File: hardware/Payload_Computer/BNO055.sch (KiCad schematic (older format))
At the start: 8 parts

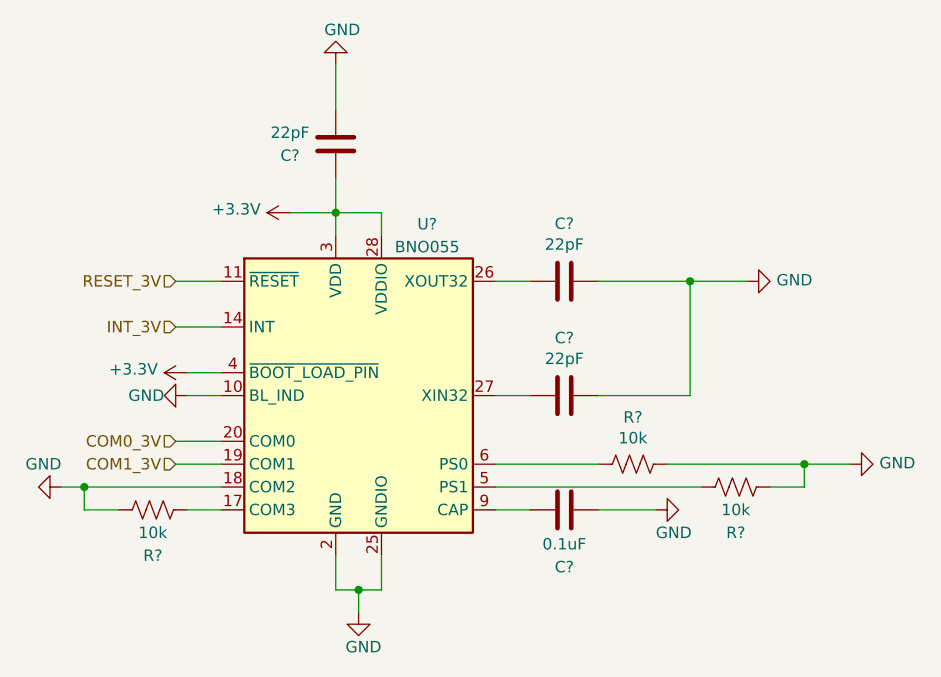
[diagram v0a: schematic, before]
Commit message: Finished BNO055
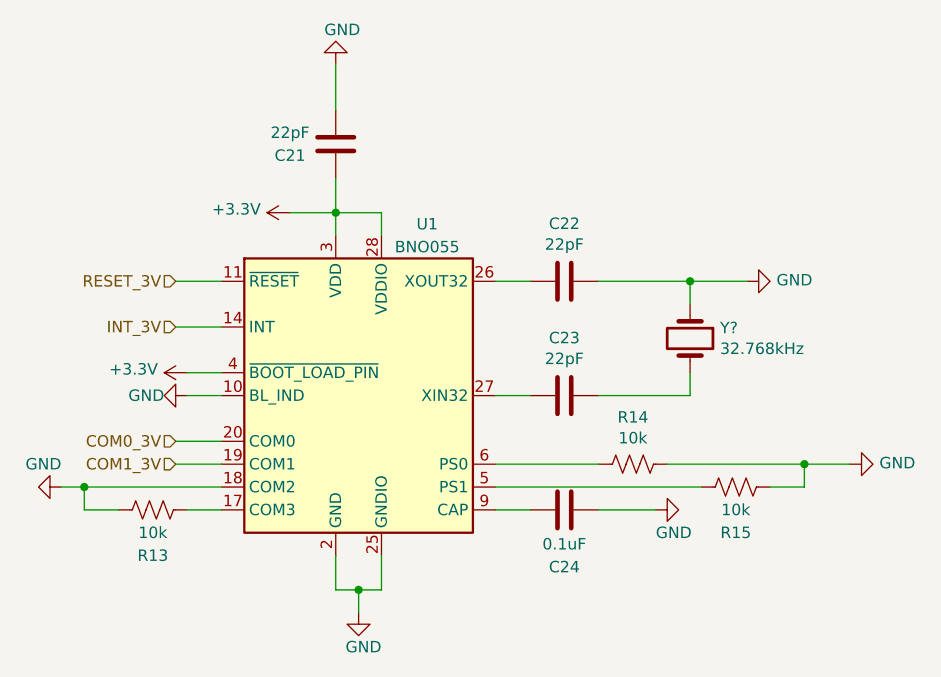
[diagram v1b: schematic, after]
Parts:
- added Y?: 32.768kHz, symbol Device:Crystal
- gave numbers to parts that had none: 8
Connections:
- net GND: now also Y?.1; no longer C23.1
- new net: C23.1, Y?.2
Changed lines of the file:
@@
 $Descr A4 11693 8268
 encoding utf-8
-Sheet 15 17
+Sheet 15 16
 Title ""
 Date ""
@@
 $EndDescr
 $Comp
-L Sensor_Motion:BNO055 U?
+L Sensor_Motion:BNO055 U1
 U 1 1 5F9DBC78
 P 5500 3750
-F 0 "U?" H 5800 4500 50  0000 C CNN
+F 0 "U1" H 5800 4500 50  0000 C CNN
 F 1 "BNO055" H 5800 4400 50  0000 C CNN
 F 2 "Package_LGA:LGA-28_5.2x3.8mm_P0.5mm" H 5750 3100 50  0001 L CNN
@@
 Connection ~ 6950 3250
 $Comp
-L power:GND #PWR?
+L power:GND #PWR0143
 U 1 1 5F9DBC80
 P 7200 3250
-F 0 "#PWR?" H 7200 3000 50  0001 C CNN
+F 0 "#PWR0143" H 7200 3000 50  0001 C CNN
 F 1 "GND" V 7205 3122 50  0000 R CNN
 F 2 "" H 7200 3250 50  0001 C CNN
@@
 Wire Wire Line
 	6100 3750 6250 3750
-Wire Wire Line
-	6950 3250 6950 3750
-$Comp
-L Device:C C?
+$Comp
+L Device:C C22
 U 1 1 5F9DBC88
 P 6400 3250
-F 0 "C?" V 6148 3250 50  0000 C CNN
+F 0 "C22" V 6148 3250 50  0000 C CNN
 F 1 "22pF" V 6239 3250 50  0000 C CNN
 F 2 "" H 6438 3100 50  0001 C CNN
@@
 $EndComp
 $Comp
-L Device:C C?
+L Device:C C24
 U 1 1 5F9DBC8E
 P 6400 4250
-F 0 "C?" V 6650 4250 50  0000 C CNN
+F 0 "C24" V 6650 4250 50  0000 C CNN
 F 1 "0.1uF" V 6550 4250 50  0000 C CNN
 F 2 "" H 6438 4100 50  0001 C CNN
@@
 	6550 4250 6800 4250
 $Comp
-L power:GND #PWR?
-U 1 1 5F9DBC99
-P 6800 4250
-F 0 "#PWR?" H 6800 4000 50  0001 C CNN
-F 1 "GND" V 6700 4250 50  0000 R CNN
-F 2 "" H 6800 4250 50  0001 C CNN
-F 3 "" H 6800 4250 50  0001 C CNN
-	1    6800 4250
-	0    -1   -1   0
-$EndComp
-$Comp
-L Device:R_US R?
+L Device:R_US R14
 U 1 1 5F9DBC9F
 P 6700 4050
-F 0 "R?" V 6495 4050 50  0000 C CNN
+F 0 "R14" V 6495 4050 50  0000 C CNN
 F 1 "10k" V 6586 4050 50  0000 C CNN
 F 2 "" V 6740 4040 50  0001 C CNN
@@
 $EndComp
 $Comp
-L Device:R_US R?
+L Device:R_US R15
 U 1 1 5F9DBCA5
 P 7150 4150
-F 0 "R?" V 7350 4150 50  0000 C CNN
+F 0 "R15" V 7350 4150 50  0000 C CNN
 F 1 "10k" V 7250 4150 50  0000 C CNN
 F 2 "" V 7190 4140 50  0001 C CNN
@@
 Connection ~ 7450 4050
 $Comp
-L power:GND #PWR?
+L power:GND #PWR0145
 U 1 1 5F9DBCB2
 P 7650 4050
-F 0 "#PWR?" H 7650 3800 50  0001 C CNN
+F 0 "#PWR0145" H 7650 3800 50  0001 C CNN
 F 1 "GND" V 7655 3922 50  0000 R CNN
 F 2 "" H 7650 4050 50  0001 C CNN
@@
 $EndComp
 $Comp
-L Device:C C?
+L Device:C C23
 U 1 1 5F9DBCB8
 P 6400 3750
-F 0 "C?" V 6148 3750 50  0000 C CNN
+F 0 "C23" V 6148 3750 50  0000 C CNN
 F 1 "22pF" V 6239 3750 50  0000 C CNN
 F 2 "" H 6438 3600 50  0001 C CNN
@@
 	4900 4150 4300 4150
 $Comp
-L power:GND #PWR?
+L power:GND #PWR0146
 U 1 1 5F9DBCBF
 P 4200 4150
-F 0 "#PWR?" H 4200 3900 50  0001 C CNN
+F 0 "#PWR0146" H 4200 3900 50  0001 C CNN
 F 1 "GND" V 4100 4150 50  0000 R CNN
 F 2 "" H 4200 4150 50  0001 C CNN
@@
 	4300 4150 4200 4150
 $Comp
-L Device:R_US R?
+L Device:R_US R13
 U 1 1 5F9DBCC9
 P 4600 4250
-F 0 "R?" V 4800 4250 50  0000 C CNN
+F 0 "R13" V 4800 4250 50  0000 C CNN
 F 1 "10k" V 4700 4250 50  0000 C CNN
 F 2 "" V 4640 4240 50  0001 C CNN
@@
 	4450 4250 4300 4250
 $Comp
-L Device:C C?
+L Device:C C21
 U 1 1 5F9DBCD0
 P 5400 2650
-F 0 "C?" H 5600 2700 50  0000 C CNN
+F 0 "C21" H 5600 2700 50  0000 C CNN
 F 1 "22pF" H 5600 2600 50  0000 C CNN
 F 2 "" H 5438 2500 50  0001 C CNN
@@
 $EndComp
 $Comp
-L power:GND #PWR?
+L power:GND #PWR0147
 U 1 1 5F9DBCD6
 P 5400 2300
-F 0 "#PWR?" H 5400 2050 50  0001 C CNN
+F 0 "#PWR0147" H 5400 2050 50  0001 C CNN
 F 1 "GND" H 5450 2150 50  0000 R CNN
 F 2 "" H 5400 2300 50  0001 C CNN
@@
 	5400 2950 5200 2950
 $Comp
-L power:+3.3V #PWR?
+L power:+3.3V #PWR0148
 U 1 1 5F9DBCE3
 P 5200 2950
-F 0 "#PWR?" H 5200 2800 50  0001 C CNN
+F 0 "#PWR0148" H 5200 2800 50  0001 C CNN
 F 1 "+3.3V" V 5215 3078 50  0000 L CNN
 F 2 "" H 5200 2950 50  0001 C CNN
@@
 	5500 4600 5600 4600
 $Comp
-L power:GND #PWR?
+L power:GND #PWR0149
 U 1 1 5F9DBCEF
 P 5500 4700
-F 0 "#PWR?" H 5500 4450 50  0001 C CNN
+F 0 "#PWR0149" H 5500 4450 50  0001 C CNN
 F 1 "GND" H 5600 4550 50  0000 R CNN
 F 2 "" H 5500 4700 50  0001 C CNN
@@
 	4900 3650 4750 3650
 $Comp
-L power:GND #PWR?
+L power:GND #PWR0150
 U 1 1 5F9DBCF7
 P 4750 3750
-F 0 "#PWR?" H 4750 3500 50  0001 C CNN
+F 0 "#PWR0150" H 4750 3500 50  0001 C CNN
 F 1 "GND" V 4750 3650 50  0000 R CNN
 F 2 "" H 4750 3750 50  0001 C CNN
@@
 $EndComp
 $Comp
-L power:+3.3V #PWR?
+L power:+3.3V #PWR0151
 U 1 1 5F9DBCFD
 P 4750 3650
-F 0 "#PWR?" H 4750 3500 50  0001 C CNN
+F 0 "#PWR0151" H 4750 3500 50  0001 C CNN
 F 1 "+3.3V" V 4765 3778 50  0000 L CNN
 F 2 "" H 4750 3650 50  0001 C CNN
@@
 Text HLabel 4700 4050 0    50   Input ~ 0
 COM1_3V
+Wire Wire Line
+	6950 3250 6950 3350
+$Comp
+L power:GND #PWR0144
+U 1 1 5F9DBC99
+P 6800 4250
+F 0 "#PWR0144" H 6800 4000 50  0001 C CNN
+F 1 "GND" V 6700 4250 50  0000 R CNN
+F 2 "" H 6800 4250 50  0001 C CNN
+F 3 "" H 6800 4250 50  0001 C CNN
+	1    6800 4250
+	0    -1   -1   0
+$EndComp
+$Comp
+L Device:Crystal Y?
+U 1 1 5FA07119
+P 6950 3500
+F 0 "Y?" V 6904 3631 50  0000 L CNN
+F 1 "32.768kHz" V 6995 3631 50  0000 L CNN
+F 2 "" H 6950 3500 50  0001 C CNN
+F 3 "~" H 6950 3500 50  0001 C CNN
+	1    6950 3500
+	0    1    1    0
+$EndComp
+Wire Wire Line
+	6950 3650 6950 3750
 $EndSCHEMATC
